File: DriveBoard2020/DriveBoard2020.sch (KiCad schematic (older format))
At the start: 46 parts, among them SW1 SW_DPST_x2, SW2 SW_Push_Dual_x2, SW3 SW_Push_Dual_x2, SW4 SW_Push_Dual_x2, U1 MAX232, U2 MAX232, U3 OKI, U4 TM4C129E_Launchpad, U5 MAX232

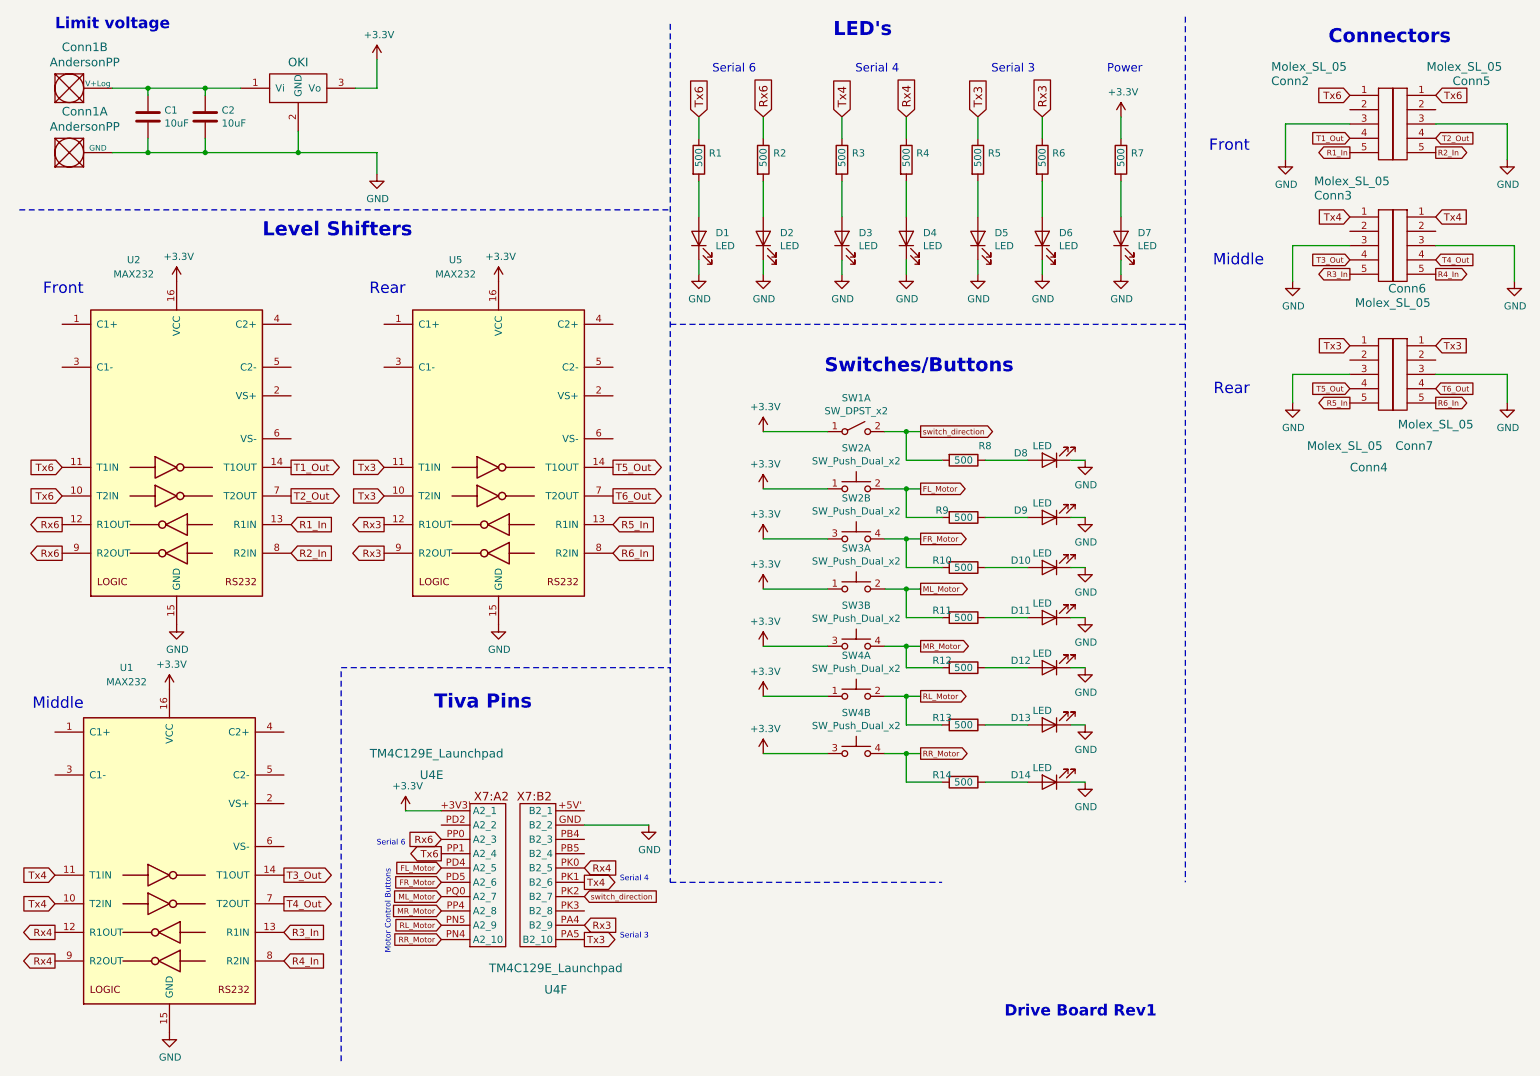
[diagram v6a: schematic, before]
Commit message: added capacitors to level shifters, added oki for 5v, finished assigning footprints
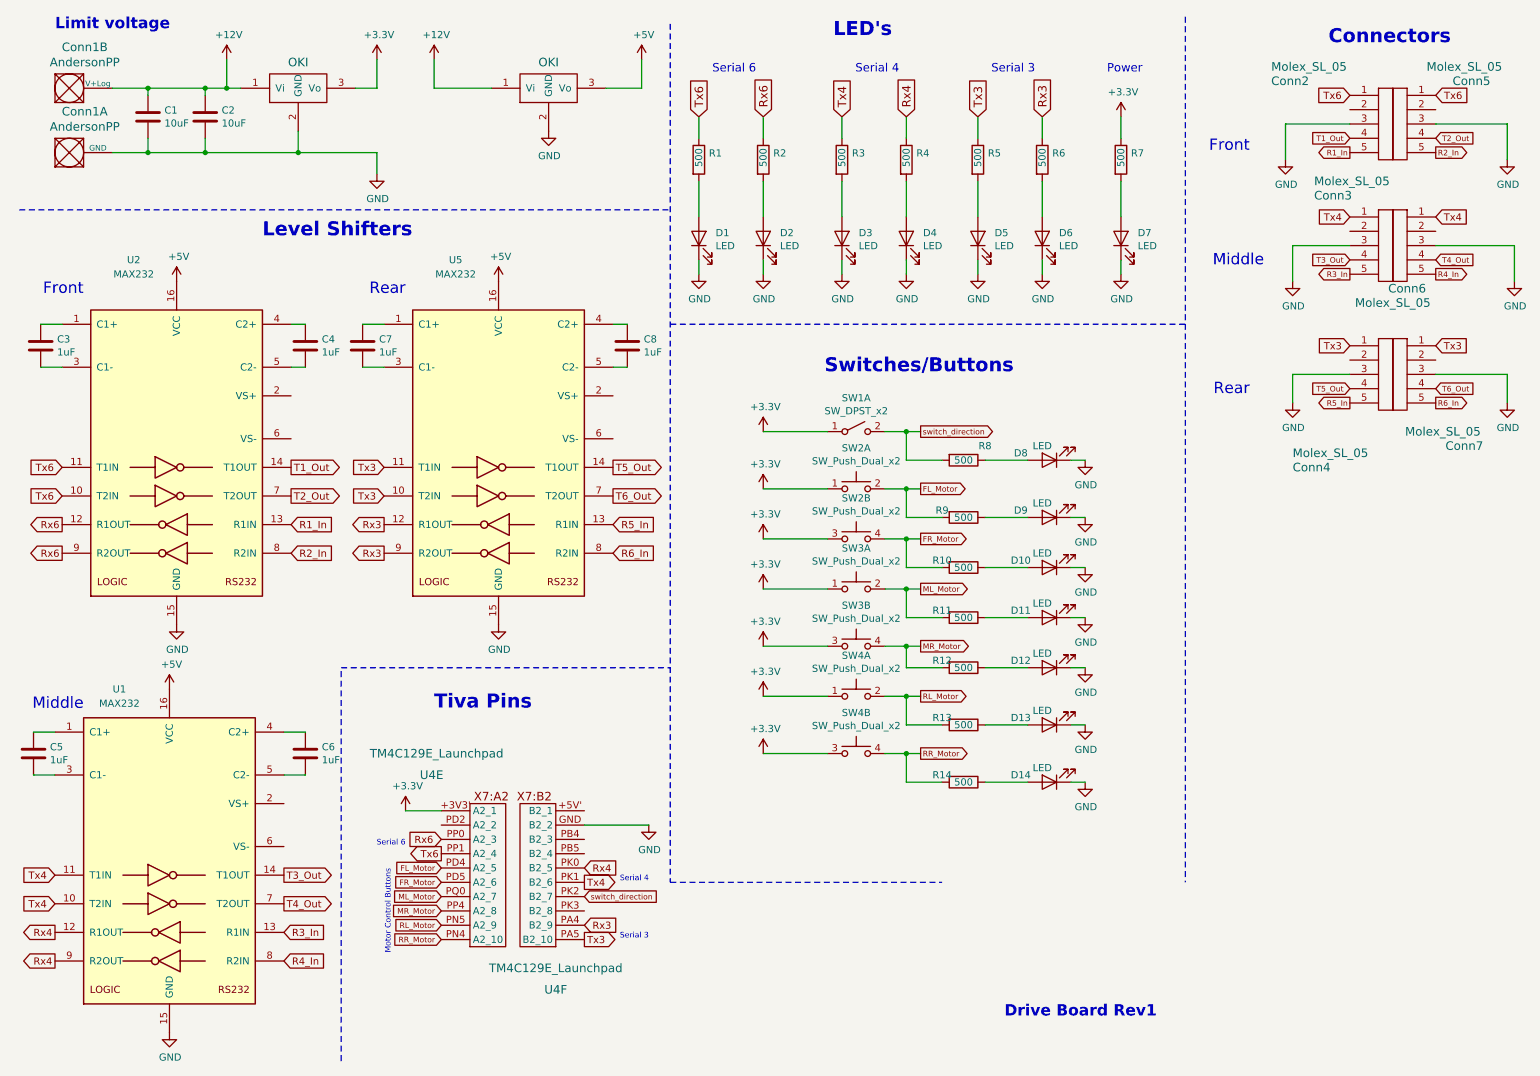
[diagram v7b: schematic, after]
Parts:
- added C3, C4, C5, C6, C7, C8: 1uF, Capacitor_SMD:C_0603_1608Metric_Pad1.05x0.95mm_HandSolder, symbol Device:C
- added U6: OKI, MRDT_Devices:OKI_Horizontal, symbol MRDT_Devices:OKI
- SW1: footprint (none) -> Button_Switch_THT:SW_CuK_OS102011MA1QN1_SPDT_Angled
- SW2, SW3, SW4: footprint (none) -> Button_Switch_SMD:SW_SPST_TL3305A
- U1, U2, U5: footprint (none) -> Package_SO:SOIC-16_3.9x9.9mm_P1.27mm
- U4: footprint (none) -> MRDT_Shields:TM4C129E_Launchpad_X7_THT_BOTTOM
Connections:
- net +3V3: no longer U1.16 (VCC), U2.16 (VCC), U5.16 (VCC)
- net GND: now also U6.2 (GND)
- net +12V: now reaches C1.1, C2.1, Conn1.2 (V+Log), U3.1 (Vi)
- net +12V: now also U6.1 (Vi)
- net at U2.1 (C1+): now also C3.1
- net at U2.3 (C1-): now also C3.2
- net at U2.4 (C2+): now also C4.1
- net at U2.5 (C2-): now also C4.2
- net at U1.1 (C1+): now also C5.1
- net at U1.3 (C1-): now also C5.2
- net at U1.4 (C2+): now also C6.1
- net at U1.5 (C2-): now also C6.2
- net at U5.1 (C1+): now also C7.1
- net at U5.3 (C1-): now also C7.2
- net at U5.4 (C2+): now also C8.1
- net at U5.5 (C2-): now also C8.2
- new net +5V: U1.16 (VCC), U2.16 (VCC), U5.16 (VCC), U6.3 (Vo)
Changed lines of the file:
@@
 Connection ~ 1800 1000
-Wire Wire Line
-	1800 1000 2050 1000
 Wire Wire Line
 	1800 1350 1800 1450
@@
 F 0 "U4" H 3300 8200 60  0000 L CNN
 F 1 "TM4C129E_Launchpad" H 2950 8350 60  0000 L CNN
-F 2 "" H 3650 7000 60  0001 C CNN
+F 2 "MRDT_Shields:TM4C129E_Launchpad_X7_THT_BOTTOM" H 3650 7000 60  0001 C CNN
 F 3 "" H 3650 7000 60  0001 C CNN
 	5    3650 7000
@@
 F 0 "U4" H 4250 6700 60  0000 C CNN
 F 1 "TM4C129E_Launchpad" H 4250 6850 60  0000 C CNN
-F 2 "" H 4250 7000 60  0001 C CNN
+F 2 "MRDT_Shields:TM4C129E_Launchpad_X7_THT_BOTTOM" H 4250 7000 60  0001 C CNN
 F 3 "" H 4250 7000 60  0001 C CNN
 	6    4250 7000
@@
 F 0 "U2" H 1300 4900 50  0000 C CNN
 F 1 "MAX232" H 1300 4800 50  0000 C CNN
-F 2 "" H 1650 2500 50  0001 L CNN
+F 2 "Package_SO:SOIC-16_3.9x9.9mm_P1.27mm" H 1650 2500 50  0001 L CNN
 F 3 "http://www.ti.com/lit/ds/symlink/max232.pdf" H 1600 3650 50  0001 C CNN
 	1    1600 3550
-	1    0    0    -1
-$EndComp
-$Comp
-L power:+3.3V #PWR0105
-U 1 1 5DA1BFEE
-P 1600 2350
-F 0 "#PWR0105" H 1600 2200 50  0001 C CNN
-F 1 "+3.3V" H 1615 2523 50  0000 C CNN
-F 2 "" H 1600 2350 50  0001 C CNN
-F 3 "" H 1600 2350 50  0001 C CNN
-	1    1600 2350
 	1    0    0    -1
 $EndComp
@@
 U 1 1 5DA3934F
 P 1550 6400
-F 0 "U1" H 1250 7750 50  0000 C CNN
-F 1 "MAX232" H 1250 7650 50  0000 C CNN
-F 2 "" H 1600 5350 50  0001 L CNN
+F 0 "U1" H 1200 7600 50  0000 C CNN
+F 1 "MAX232" H 1200 7500 50  0000 C CNN
+F 2 "Package_SO:SOIC-16_3.9x9.9mm_P1.27mm" H 1600 5350 50  0001 L CNN
 F 3 "http://www.ti.com/lit/ds/symlink/max232.pdf" H 1550 6500 50  0001 C CNN
 	1    1550 6400
-	1    0    0    -1
-$EndComp
-$Comp
-L power:+3.3V #PWR0107
-U 1 1 5DA3C5B3
-P 1550 5200
-F 0 "#PWR0107" H 1550 5050 50  0001 C CNN
-F 1 "+3.3V" H 1565 5373 50  0000 C CNN
-F 2 "" H 1550 5200 50  0001 C CNN
-F 3 "" H 1550 5200 50  0001 C CNN
-	1    1550 5200
 	1    0    0    -1
 $EndComp
@@
 R6_In
 $Comp
-L power:+3.3V #PWR0109
-U 1 1 5DA61775
-P 3850 2350
-F 0 "#PWR0109" H 3850 2200 50  0001 C CNN
-F 1 "+3.3V" H 3865 2523 50  0000 C CNN
-F 2 "" H 3850 2350 50  0001 C CNN
-F 3 "" H 3850 2350 50  0001 C CNN
-	1    3850 2350
-	1    0    0    -1
-$EndComp
-$Comp
 L power:GND #PWR0110
 U 1 1 5DA6275E
@@
 F 0 "U5" H 3550 4900 50  0000 C CNN
 F 1 "MAX232" H 3550 4800 50  0000 C CNN
-F 2 "" H 3900 2500 50  0001 L CNN
+F 2 "Package_SO:SOIC-16_3.9x9.9mm_P1.27mm" H 3900 2500 50  0001 L CNN
 F 3 "http://www.ti.com/lit/ds/symlink/max232.pdf" H 3850 3650 50  0001 C CNN
 	1    3850 3550
@@
 U 1 1 5D9F0E09
 P 10000 3250
-F 0 "Conn4" H 9800 2850 60  0000 L CNN
-F 1 "Molex_SL_05" H 9500 3000 60  0000 L CNN
+F 0 "Conn4" H 9400 2850 60  0000 L CNN
+F 1 "Molex_SL_05" H 9400 2950 60  0000 L CNN
 F 2 "MRDT_Connectors:MOLEX_SL_05_Horizontal" H 10000 3250 60  0001 C CNN
 F 3 "" H 10000 3250 60  0001 C CNN
@@
 U 1 1 5DA45098
 P 10200 3250
-F 0 "Conn7" H 10150 3000 60  0000 C CNN
-F 1 "Molex_SL_05" H 10000 3150 60  0000 C CNN
+F 0 "Conn7" H 9800 3000 60  0000 C CNN
+F 1 "Molex_SL_05" H 9950 3100 60  0000 C CNN
 F 2 "MRDT_Connectors:MOLEX_SL_05_Horizontal" H 10200 3250 60  0001 C CNN
 F 3 "" H 10200 3250 60  0001 C CNN
@@
 F 0 "SW1" H 6350 3635 50  0000 C CNN
 F 1 "SW_DPST_x2" H 6350 3544 50  0000 C CNN
-F 2 "" H 6350 3400 50  0001 C CNN
+F 2 "Button_Switch_THT:SW_CuK_OS102011MA1QN1_SPDT_Angled" H 6350 3400 50  0001 C CNN
 F 3 "~" H 6350 3400 50  0001 C CNN
 	1    6350 3400
@@
 F 0 "SW2" H 6350 4085 50  0000 C CNN
 F 1 "SW_Push_Dual_x2" H 6350 3994 50  0000 C CNN
-F 2 "" H 6350 4000 50  0001 C CNN
+F 2 "Button_Switch_SMD:SW_SPST_TL3305A" H 6350 4000 50  0001 C CNN
 F 3 "~" H 6350 4000 50  0001 C CNN
 	1    6350 3800
@@
 F 0 "SW2" H 6350 4435 50  0000 C CNN
 F 1 "SW_Push_Dual_x2" H 6350 4344 50  0000 C CNN
-F 2 "" H 6350 4350 50  0001 C CNN
+F 2 "Button_Switch_SMD:SW_SPST_TL3305A" H 6350 4350 50  0001 C CNN
 F 3 "~" H 6350 4350 50  0001 C CNN
 	2    6350 4150
@@
 F 0 "SW3" H 6350 4785 50  0000 C CNN
 F 1 "SW_Push_Dual_x2" H 6350 4694 50  0000 C CNN
-F 2 "" H 6350 4700 50  0001 C CNN
+F 2 "Button_Switch_SMD:SW_SPST_TL3305A" H 6350 4700 50  0001 C CNN
 F 3 "~" H 6350 4700 50  0001 C CNN
 	1    6350 4500
@@
 F 0 "SW3" H 6350 5185 50  0000 C CNN
 F 1 "SW_Push_Dual_x2" H 6350 5094 50  0000 C CNN
-F 2 "" H 6350 5100 50  0001 C CNN
+F 2 "Button_Switch_SMD:SW_SPST_TL3305A" H 6350 5100 50  0001 C CNN
 F 3 "~" H 6350 5100 50  0001 C CNN
 	2    6350 4900
@@
 F 0 "SW4" H 6350 5535 50  0000 C CNN
 F 1 "SW_Push_Dual_x2" H 6350 5444 50  0000 C CNN
-F 2 "" H 6350 5450 50  0001 C CNN
+F 2 "Button_Switch_SMD:SW_SPST_TL3305A" H 6350 5450 50  0001 C CNN
 F 3 "~" H 6350 5450 50  0001 C CNN
 	1    6350 5250
@@
 F 0 "SW4" H 6350 5935 50  0000 C CNN
 F 1 "SW_Push_Dual_x2" H 6350 5844 50  0000 C CNN
-F 2 "" H 6350 5850 50  0001 C CNN
+F 2 "Button_Switch_SMD:SW_SPST_TL3305A" H 6350 5850 50  0001 C CNN
 F 3 "~" H 6350 5850 50  0001 C CNN
 	2    6350 5650
@@
 Wire Notes Line style solid
 	5050 550  5050 6550
+$Comp
+L power:+12V #PWR0105
+U 1 1 5D9FDEF2
+P 1950 800
+F 0 "#PWR0105" H 1950 650 50  0001 C CNN
+F 1 "+12V" H 1965 973 50  0000 C CNN
+F 2 "" H 1950 800 50  0001 C CNN
+F 3 "" H 1950 800 50  0001 C CNN
+	1    1950 800
+	1    0    0    -1
+$EndComp
+$Comp
+L power:+12V #PWR0107
+U 1 1 5D9FF58C
+P 3400 800
+F 0 "#PWR0107" H 3400 650 50  0001 C CNN
+F 1 "+12V" H 3415 973 50  0000 C CNN
+F 2 "" H 3400 800 50  0001 C CNN
+F 3 "" H 3400 800 50  0001 C CNN
+	1    3400 800
+	1    0    0    -1
+$EndComp
+Wire Wire Line
+	3400 1000 3800 1000
+$Comp
+L MRDT_Devices:OKI U6
+U 1 1 5DA04040
+P 4000 1100
+F 0 "U6" H 4050 1050 60  0001 C CNN
+F 1 "OKI" H 4200 1381 60  0000 C CNN
+F 2 "MRDT_Devices:OKI_Horizontal" H 3800 1000 60  0001 C CNN
+F 3 "" H 3800 1000 60  0001 C CNN
+	1    4000 1100
+	1    0    0    -1
+$EndComp
+Wire Wire Line
+	4600 1000 4850 1000
+$Comp
+L power:+5V #PWR0109
+U 1 1 5DA0AFD2
+P 4850 800
+F 0 "#PWR0109" H 4850 650 50  0001 C CNN
+F 1 "+5V" H 4865 973 50  0000 C CNN
+F 2 "" H 4850 800 50  0001 C CNN
+F 3 "" H 4850 800 50  0001 C CNN
+	1    4850 800
+	1    0    0    -1
+$EndComp
+$Comp
+L power:GND #PWR0139
+U 1 1 5DA0B766
+P 4200 1300
+F 0 "#PWR0139" H 4200 1050 50  0001 C CNN
+F 1 "GND" H 4205 1127 50  0000 C CNN
+F 2 "" H 4200 1300 50  0001 C CNN
+F 3 "" H 4200 1300 50  0001 C CNN
+	1    4200 1300
+	1    0    0    -1
+$EndComp
+Wire Wire Line
+	1800 1000 1950 1000
+Wire Wire Line
+	1950 1000 1950 800
+Connection ~ 1950 1000
+Wire Wire Line
+	1950 1000 2050 1000
+Wire Wire Line
+	3400 1000 3400 800
+Wire Wire Line
+	4850 1000 4850 800
+$Comp
+L power:+5V #PWR0140
+U 1 1 5DA3112E
+P 1600 2350
+F 0 "#PWR0140" H 1600 2200 50  0001 C CNN
+F 1 "+5V" H 1615 2523 50  0000 C CNN
+F 2 "" H 1600 2350 50  0001 C CNN
+F 3 "" H 1600 2350 50  0001 C CNN
+	1    1600 2350
+	1    0    0    -1
+$EndComp
+$Comp
+L power:+5V #PWR0141
+U 1 1 5DA327C3
+P 3850 2350
+F 0 "#PWR0141" H 3850 2200 50  0001 C CNN
+F 1 "+5V" H 3865 2523 50  0000 C CNN
+F 2 "" H 3850 2350 50  0001 C CNN
+F 3 "" H 3850 2350 50  0001 C CNN
+	1    3850 2350
+	1    0    0    -1
+$EndComp
+$Comp
+L power:+5V #PWR0142
+U 1 1 5DA32D14
+P 1550 5200
+F 0 "#PWR0142" H 1550 5050 50  0001 C CNN
+F 1 "+5V" H 1565 5373 50  0000 C CNN
+F 2 "" H 1550 5200 50  0001 C CNN
+F 3 "" H 1550 5200 50  0001 C CNN
+	1    1550 5200
+	1    0    0    -1
+$EndComp
+$Comp
+L Device:C C5
+U 1 1 5DA341A4
+P 600 5650
+F 0 "C5" H 715 5696 50  0000 L CNN
+F 1 "1uF" H 715 5605 50  0000 L CNN
+F 2 "Capacitor_SMD:C_0603_1608Metric_Pad1.05x0.95mm_HandSolder" H 638 5500 50  0001 C CNN
+F 3 "~" H 600 5650 50  0001 C CNN
+	1    600  5650
+	1    0    0    -1
+$EndComp
+$Comp
+L Device:C C6
+U 1 1 5DA3488F
+P 2500 5650
+F 0 "C6" H 2615 5696 50  0000 L CNN
+F 1 "1uF" H 2615 5605 50  0000 L CNN
+F 2 "Capacitor_SMD:C_0603_1608Metric_Pad1.05x0.95mm_HandSolder" H 2538 5500 50  0001 C CNN
+F 3 "~" H 2500 5650 50  0001 C CNN
+	1    2500 5650
+	1    0    0    -1
+$EndComp
+Wire Wire Line
+	2500 5500 2350 5500
+Wire Wire Line
+	2500 5800 2350 5800
+Wire Wire Line
+	750  5800 600  5800
+Wire Wire Line
+	600  5500 750  5500
+$Comp
+L Device:C C3
+U 1 1 5DA4304E
+P 650 2800
+F 0 "C3" H 765 2846 50  0000 L CNN
+F 1 "1uF" H 765 2755 50  0000 L CNN
+F 2 "Capacitor_SMD:C_0603_1608Metric_Pad1.05x0.95mm_HandSolder" H 688 2650 50  0001 C CNN
+F 3 "~" H 650 2800 50  0001 C CNN
+	1    650  2800
+	1    0    0    -1
+$EndComp
+$Comp
+L Device:C C4
+U 1 1 5DA43AF8
+P 2500 2800
+F 0 "C4" H 2615 2846 50  0000 L CNN
+F 1 "1uF" H 2615 2755 50  0000 L CNN
+F 2 "Capacitor_SMD:C_0603_1608Metric_Pad1.05x0.95mm_HandSolder" H 2538 2650 50  0001 C CNN
+F 3 "~" H 2500 2800 50  0001 C CNN
+	1    2500 2800
+	1    0    0    -1
+$EndComp
+$Comp
+L Device:C C7
+U 1 1 5DA43FB3
+P 2900 2800
+F 0 "C7" H 3015 2846 50  0000 L CNN
+F 1 "1uF" H 3015 2755 50  0000 L CNN
+F 2 "Capacitor_SMD:C_0603_1608Metric_Pad1.05x0.95mm_HandSolder" H 2938 2650 50  0001 C CNN
+F 3 "~" H 2900 2800 50  0001 C CNN
+	1    2900 2800
+	1    0    0    -1
+$EndComp
+$Comp
+L Device:C C8
+U 1 1 5DA44EFA
+P 4750 2800
+F 0 "C8" H 4865 2846 50  0000 L CNN
+F 1 "1uF" H 4865 2755 50  0000 L CNN
+F 2 "Capacitor_SMD:C_0603_1608Metric_Pad1.05x0.95mm_HandSolder" H 4788 2650 50  0001 C CNN
+F 3 "~" H 4750 2800 50  0001 C CNN
+	1    4750 2800
+	1    0    0    -1
+$EndComp
+Wire Wire Line
+	4750 2650 4650 2650
+Wire Wire Line
+	4750 2950 4650 2950
+Wire Wire Line
+	2900 2650 3050 2650
+Wire Wire Line
+	2900 2950 3050 2950
+Wire Wire Line
+	2400 2650 2500 2650
+Wire Wire Line
+	2400 2950 2500 2950
+Wire Wire Line
+	800  2650 650  2650
+Wire Wire Line
+	650  2950 800  2950
 $EndSCHEMATC
